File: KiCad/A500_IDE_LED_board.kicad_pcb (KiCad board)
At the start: 2 copper layers, 25.4 x 18 mm, 10 parts, among them J1 Conn_01x08, J2 Conn_01x08, J3 Conn_01x01, J4 Conn_01x01, Q1 BC857C, U1 74HCT2G14

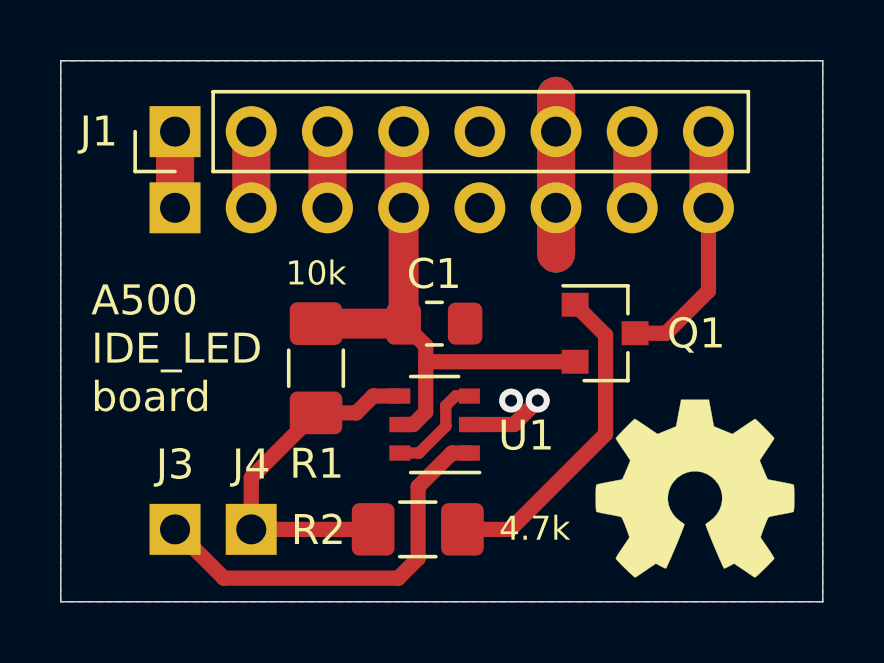
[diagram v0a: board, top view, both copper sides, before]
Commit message: elongated J3-pad, and did some silkscreen fixes
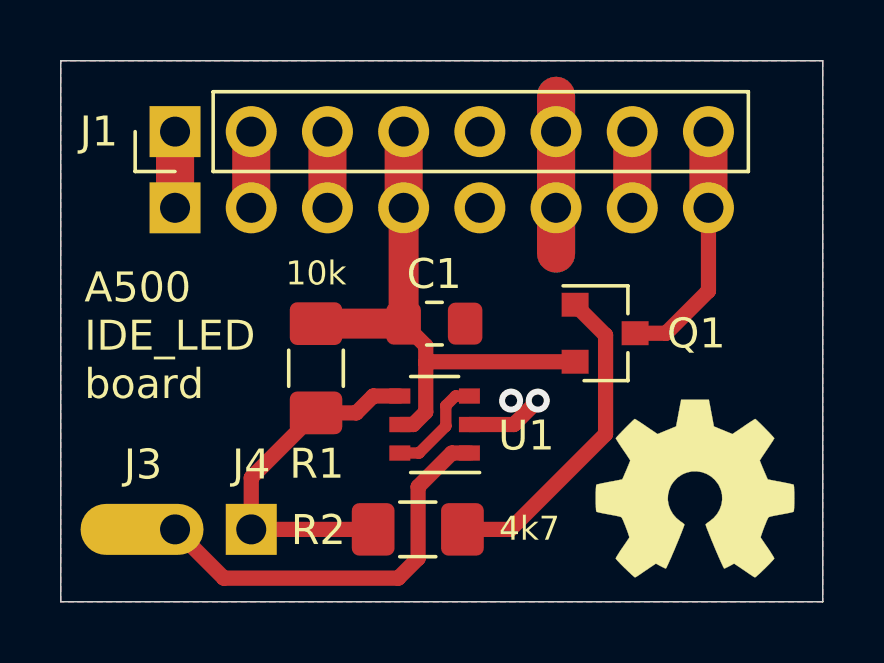
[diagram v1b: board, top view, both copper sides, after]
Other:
- board text added: "4k7"
- board text removed: "4.7k"

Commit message: added Revision to silkscreen
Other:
- board text added: "Rev. A"
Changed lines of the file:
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@@
   (general
     (thickness 1.6)
-    (drawings 7)
+    (drawings 8)
     (tracks 45)
     (zones 0)
@@
     )
   )
+  (gr_text "Rev. A" (at 138.4554 102.5144) (layer B.SilkS)
+    (effects (font (size 1.5 1.5) (thickness 0.15)) (justify mirror))
+  )
   (gr_text 4k7 (at 135.001 102.4636) (layer F.SilkS)

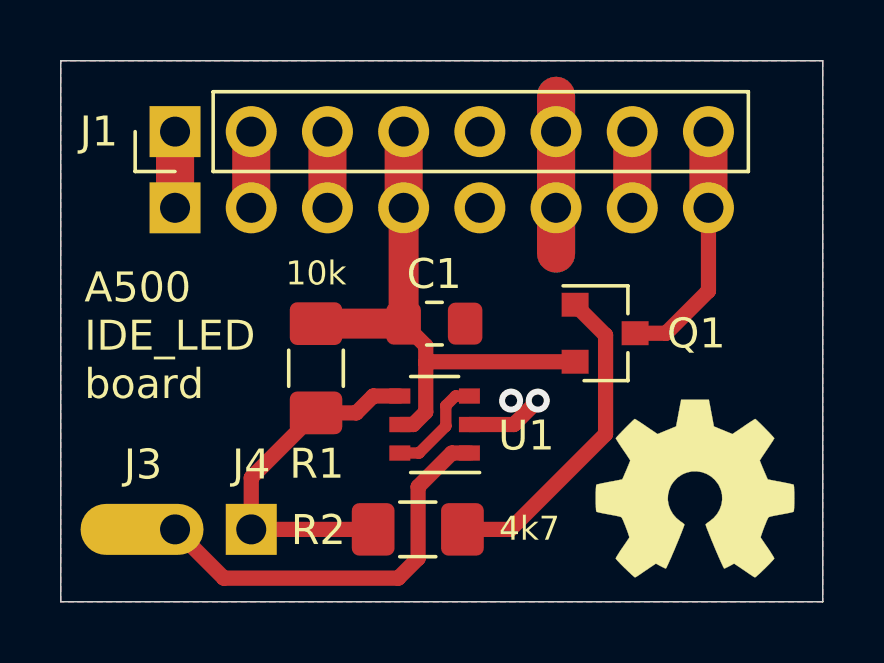
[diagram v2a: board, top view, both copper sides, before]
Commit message: re-positioned J4 next to J3 and elongated pad
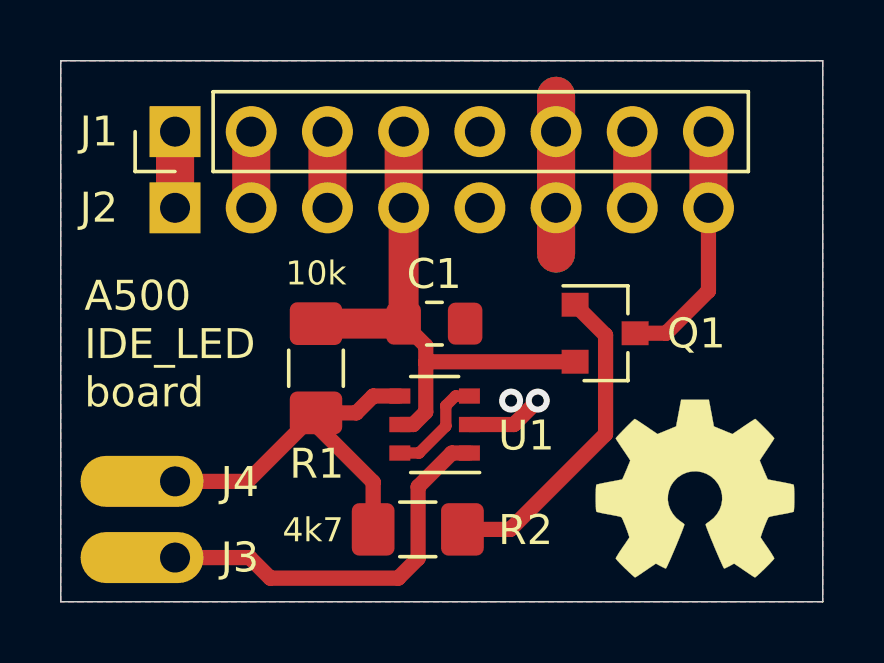
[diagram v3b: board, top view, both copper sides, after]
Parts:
- J4: footprint Connector_PinHeader_2.54mm:PinHeader_1x01_P2.54mm_Vertical -> Connector_PinHeader_2.54mm:PinHeader_1x01_P2.54mm_Horizontal
- moved J4 3.00 mm to (123.2, 100.9), turned to 180 degrees
- moved J3 0.94 mm to (123.2, 103.4)
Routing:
- net ACTIVE: track 11.9 -> 13.3 mm
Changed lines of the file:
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@@
     (thickness 1.6)
     (drawings 8)
-    (tracks 45)
+    (tracks 48)
     (zones 0)
     (modules 10)
@@
   )
   (setup
-    (last_trace_width 0.25)
+    (last_trace_width 0.508)
     (user_trace_width 0.254)
     (user_trace_width 0.381)
@@
   )
   (module Connector_PinHeader_2.54mm:PinHeader_1x01_P2.54mm_Horizontal (layer F.Cu)
-    (at 123.19 102.489 180)
+    (at 123.19 100.8888 180)
     (descr "Through hole angled pin header, 1x01, 2.54mm pitch, 6mm pin length, single row")
     (tags "Through hole angled pin header THT 1x01 2.54mm single row")
-    (fp_text reference J3 (at 1.0668 2.159 180) (layer F.SilkS)
+    (fp_text reference J4 (at -2.159 -0.0254 180) (layer F.SilkS)
+      (effects (font (size 1 1) (thickness 0.15)))
+    )
+    (fp_text value Conn_01x01 (at 4.385 2.27 180) (layer F.Fab) hide
+      (effects (font (size 1 1) (thickness 0.15)))
+    )
+    (fp_text user %R (at 2.77 0 270) (layer F.Fab) hide
+      (effects (font (size 1 1) (thickness 0.15)))
+    )
+    (fp_line (start 2.135 -1.27) (end 4.04 -1.27) (layer F.Fab) (width 0.1))
+    (fp_line (start 4.04 -1.27) (end 4.04 1.27) (layer F.Fab) (width 0.1))
+    (fp_line (start 4.04 1.27) (end 1.5 1.27) (layer F.Fab) (width 0.1))
+    (fp_line (start 1.5 1.27) (end 1.5 -0.635) (layer F.Fab) (width 0.1))
+    (fp_line (start 1.5 -0.635) (end 2.135 -1.27) (layer F.Fab) (width 0.1))
+    (fp_line (start -0.32 -0.32) (end 1.5 -0.32) (layer F.Fab) (width 0.1))
+    (fp_line (start -0.32 -0.32) (end -0.32 0.32) (layer F.Fab) (width 0.1))
+    (fp_line (start -0.32 0.32) (end 1.5 0.32) (layer F.Fab) (width 0.1))
+    (fp_line (start 4.04 -0.32) (end 10.04 -0.32) (layer F.Fab) (width 0.1))
+    (fp_line (start 10.04 -0.32) (end 10.04 0.32) (layer F.Fab) (width 0.1))
+    (fp_line (start 4.04 0.32) (end 10.04 0.32) (layer F.Fab) (width 0.1))
+    (fp_line (start -1.8 -1.8) (end -1.8 1.8) (layer F.CrtYd) (width 0.05))
+    (fp_line (start -1.8 1.8) (end 10.55 1.8) (layer F.CrtYd) (width 0.05))
+    (fp_line (start 10.55 1.8) (end 10.55 -1.8) (layer F.CrtYd) (width 0.05))
+    (fp_line (start 10.55 -1.8) (end -1.8 -1.8) (layer F.CrtYd) (width 0.05))
+    (pad 1 thru_hole oval (at 0 0 180) (size 4.1 1.7) (drill 1 (offset 1.1 0)) (layers *.Cu *.Mask)
+      (net 3 ACTIVE))
+    (model ${KISYS3DMOD}/Connector_PinHeader_2.54mm.3dshapes/PinHeader_1x01_P2.54mm_Horizontal.wrl
+      (at (xyz 0 0 0))
+      (scale (xyz 1 1 1))
+      (rotate (xyz 0 0 0))
+    )
+  )
+  (module Connector_PinHeader_2.54mm:PinHeader_1x01_P2.54mm_Horizontal (layer F.Cu)
+    (at 123.19 103.4288 180)
+    (descr "Through hole angled pin header, 1x01, 2.54mm pitch, 6mm pin length, single row")
+    (tags "Through hole angled pin header THT 1x01 2.54mm single row")
+    (fp_text reference J3 (at -2.159 0 180) (layer F.SilkS)
       (effects (font (size 1 1) (thickness 0.15)))
     )
@@
       (xy 0.555814 -2.531069)) (layer F.SilkS) (width 0.01))
   )
-  (module Connector_PinHeader_2.54mm:PinHeader_1x01_P2.54mm_Vertical (layer F.Cu)
-    (at 125.73 102.489)
-    (descr "Through hole straight pin header, 1x01, 2.54mm pitch, single row")
-    (tags "Through hole pin header THT 1x01 2.54mm single row")
-    (fp_text reference J4 (at 0 -2.159) (layer F.SilkS)
-      (effects (font (size 1 1) (thickness 0.15)))
-    )
-    (fp_text value Conn_01x01 (at 0 2.33) (layer F.Fab) hide
-      (effects (font (size 1 1) (thickness 0.15)))
-    )
-    (fp_line (start -0.635 -1.27) (end 1.27 -1.27) (layer F.Fab) (width 0.1))
-    (fp_line (start 1.27 -1.27) (end 1.27 1.27) (layer F.Fab) (width 0.1))
-    (fp_line (start 1.27 1.27) (end -1.27 1.27) (layer F.Fab) (width 0.1))
-    (fp_line (start -1.27 1.27) (end -1.27 -0.635) (layer F.Fab) (width 0.1))
-    (fp_line (start -1.27 -0.635) (end -0.635 -1.27) (layer F.Fab) (width 0.1))
-    (fp_line (start -1.8 -1.8) (end -1.8 1.8) (layer F.CrtYd) (width 0.05))
-    (fp_line (start -1.8 1.8) (end 1.8 1.8) (layer F.CrtYd) (width 0.05))
-    (fp_line (start 1.8 1.8) (end 1.8 -1.8) (layer F.CrtYd) (width 0.05))
-    (fp_line (start 1.8 -1.8) (end -1.8 -1.8) (layer F.CrtYd) (width 0.05))
-    (fp_text user %R (at 0 0 90) (layer F.Fab) hide
-      (effects (font (size 1 1) (thickness 0.15)))
-    )
-    (pad 1 thru_hole rect (at 0 0) (size 1.7 1.7) (drill 1) (layers *.Cu *.Mask)
-      (net 3 ACTIVE))
-  )
   (module Resistor_SMD:R_1206_3216Metric_Pad1.42x1.75mm_HandSolder (layer F.Cu)
     (at 131.2815 102.489 180)
@@
     (tags "resistor handsolder")
     (attr smd)
-    (fp_text reference R2 (at 3.3163 -0.0254) (layer F.SilkS)
+    (fp_text reference R2 (at -3.5925 -0.0254) (layer F.SilkS)
       (effects (font (size 1 1) (thickness 0.15)))
     )
@@
     (descr "Through hole straight socket strip, 1x08, 2.54mm pitch, single row (from Kicad 4.0.7), script generated")
     (tags "Through hole socket strip THT 1x08 2.54mm single row")
-    (fp_text reference J2 (at 0 2.54 180) (layer B.SilkS)
-      (effects (font (size 1 1) (thickness 0.15)) (justify mirror))
+    (fp_text reference J2 (at 0 2.54) (layer F.SilkS)
+      (effects (font (size 1 1) (thickness 0.15)))
     )
     (fp_text value Conn_01x08 (at 0 -20.55 90) (layer B.Fab) hide
@@
     (effects (font (size 1.5 1.5) (thickness 0.15)) (justify mirror))
   )
-  (gr_text 4k7 (at 135.001 102.4636) (layer F.SilkS)
+  (gr_text 4k7 (at 127.7874 102.5144) (layer F.SilkS)
     (effects (font (size 0.8 0.8) (thickness 0.15)))
   )
@@
     (effects (font (size 0.8 0.8) (thickness 0.15)))
   )
-  (gr_text "A500\nIDE_LED\nboard" (at 120.1674 96.0374) (layer F.SilkS)
+  (gr_text "A500\nIDE_LED\nboard" (at 120.1674 96.3168) (layer F.SilkS)
     (effects (font (size 1 1) (thickness 0.15)) (justify left))
   )
@@
   (segment (start 131.323 99.944) (end 132.216509 99.050491) (width 0.381) (layer F.Cu) (net 2))
   (segment (start 130.7084 99.944) (end 131.323 99.944) (width 0.381) (layer F.Cu) (net 2))
-  (segment (start 125.73 102.489) (end 129.794 102.489) (width 0.508) (layer F.Cu) (net 3))
   (segment (start 127.889 98.606) (end 129.232 98.606) (width 0.508) (layer F.Cu) (net 3))
   (segment (start 129.794 98.044) (end 130.683 98.044) (width 0.508) (layer F.Cu) (net 3))
   (segment (start 129.232 98.606) (end 129.794 98.044) (width 0.508) (layer F.Cu) (net 3))
-  (segment (start 125.73 100.765) (end 127.889 98.606) (width 0.508) (layer F.Cu) (net 3))
-  (segment (start 125.73 102.489) (end 125.73 100.765) (width 0.508) (layer F.Cu) (net 3))
+  (segment (start 125.6062 100.8888) (end 127.889 98.606) (width 0.508) (layer F.Cu) (net 3))
+  (segment (start 123.19 100.8888) (end 125.6062 100.8888) (width 0.508) (layer F.Cu) (net 3))
+  (segment (start 127.889 99.0092) (end 127.889 98.606) (width 0.508) (layer F.Cu) (net 3))
+  (segment (start 129.794 100.9142) (end 127.889 99.0092) (width 0.508) (layer F.Cu) (net 3))
+  (segment (start 129.794 102.489) (end 129.794 100.9142) (width 0.508) (layer F.Cu) (net 3))
+  (segment (start 126.365 104.1146) (end 125.6792 103.4288) (width 0.508) (layer F.Cu) (net 4))
+  (segment (start 131.2926 103.4542) (end 130.6322 104.1146) (width 0.508) (layer F.Cu) (net 4))
+  (segment (start 132.4152 99.944) (end 131.2926 101.0666) (width 0.508) (layer F.Cu) (net 4))
+  (segment (start 125.6792 103.4288) (end 123.19 103.4288) (width 0.508) (layer F.Cu) (net 4))
+  (segment (start 130.6322 104.1146) (end 126.365 104.1146) (width 0.508) (layer F.Cu) (net 4))
+  (segment (start 131.2926 101.0666) (end 131.2926 103.4542) (width 0.508) (layer F.Cu) (net 4))
   (segment (start 133.0284 99.944) (end 132.4152 99.944) (width 0.508) (layer F.Cu) (net 4))
-  (segment (start 132.4152 99.944) (end 131.2926 101.0666) (width 0.508) (layer F.Cu) (net 4))
-  (segment (start 131.2926 101.0666) (end 131.2926 103.4542) (width 0.508) (layer F.Cu) (net 4))
-  (segment (start 131.2926 103.4542) (end 130.6322 104.1146) (width 0.508) (layer F.Cu) (net 4))
-  (segment (start 124.8156 104.1146) (end 123.19 102.489) (width 0.508) (layer F.Cu) (net 4))
-  (segment (start 130.6322 104.1146) (end 124.8156 104.1146) (width 0.508) (layer F.Cu) (net 4))
   (segment (start 130.81 89.2302) (end 130.81 91.7702) (width 1.27) (layer F.Cu) (net 5))
   (segment (start 130.81 91.7702) (end 130.81 95.631) (width 1) (layer F.Cu) (net 5))
